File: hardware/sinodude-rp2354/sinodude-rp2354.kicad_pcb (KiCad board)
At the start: 2 copper layers, 0 parts

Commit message: hardware: PCB placement, 2-layer stackup and ground pours
75 x 40 mm two-layer board. J1 (USB-C), U1 (RP2354A) and J4 (DUT IDC header)
share the y=120 centreline, with signal flow left to right: USB-C, ESD, MCU,
level shifters, DUT header.

U1 is rotated 180 so its pins 4-14 (the nine level-shifter signals, the widest
bundle on the board) face U4 directly, and USB DM/DP leave the bottom-left
toward J1. Decoupling rings U1 on all four sides; the B-side series resistors
and ESD diodes stack in two columns between U4 and J4.

Netclasses follow Glasgow's revC3 values scaled for 2 layers: Default 0.2 mm
track / 0.2 mm clearance / 0.6-0.3 via, Power 0.5 mm, Fine 0.15 mm for the
0.4 mm-pitch QFN escapes. GND pours on both layers.

Placement scores clean on courtyards; the two reported outline failures are
J1 and J4 deliberately overhanging, being the USB-C mouth and the IDC shroud.
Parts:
- added C1: 100nF, Capacitor_SMD:C_0402_1005Metric, F.Cu at (108.5, 110.0)
- added C10: 100nF, Capacitor_SMD:C_0402_1005Metric, F.Cu at (131.1, 125.0)
- added C11: 100nF, Capacitor_SMD:C_0402_1005Metric, F.Cu at (133.3, 125.0)
- added C12: 100nF, Capacitor_SMD:C_0402_1005Metric, F.Cu at (125.2, 117.5)
- added C13: 100nF, Capacitor_SMD:C_0402_1005Metric, F.Cu at (134.8, 120.0)
- added C14: 100nF, Capacitor_SMD:C_0402_1005Metric, F.Cu at (129.9, 115.0)
- added C15: 100nF, Capacitor_SMD:C_0402_1005Metric, F.Cu at (125.2, 120.0)
- added C16: 100nF, Capacitor_SMD:C_0402_1005Metric, F.Cu at (134.8, 117.5)
- added C17: 100nF, Capacitor_SMD:C_0402_1005Metric, F.Cu at (134.8, 122.5)
- added C18: 100nF, Capacitor_SMD:C_0402_1005Metric, F.Cu at (125.2, 122.5)
- added C19: 10uF/6.3V/20%/X5R/C0402, Capacitor_SMD:C_0402_1005Metric, F.Cu at (136.8, 124.5)
- added C20: 4.7uF/10V/20%/X5R/C0402, Capacitor_SMD:C_0402_1005Metric, F.Cu at (126.7, 125.0)
- added C21: 4.7uF/10V/20%/X5R/C0402, Capacitor_SMD:C_0402_1005Metric, F.Cu at (119.5, 127.0)
- added C22: 15pF/50V/5%/C0G/C0603, Capacitor_SMD:C_0603_1608Metric, F.Cu at (126.0, 111.3)
- added C23: 15pF/50V/5%/C0G/C0603, Capacitor_SMD:C_0603_1608Metric, F.Cu at (135.0, 111.3)
- added C25: 100nF, Capacitor_SMD:C_0402_1005Metric, F.Cu at (121.5, 105.0)
- added C26: 100nF, Capacitor_SMD:C_0402_1005Metric, F.Cu at (121.0, 135.0)
- added C27: 10uF, Capacitor_SMD:C_0805_2012Metric, F.Cu at (148.0, 131.0)
- added C28: 100nF, Capacitor_SMD:C_0402_1005Metric, F.Cu at (152.5, 134.5)
- added C29: 100nF, Capacitor_SMD:C_0603_1608Metric, F.Cu at (130.5, 133.0)
- added C30: 100nF, Capacitor_SMD:C_0402_1005Metric, F.Cu at (140.0, 111.5)
- added C31: 100nF, Capacitor_SMD:C_0402_1005Metric, F.Cu at (149.0, 111.5)
- added C32: 100nF, Capacitor_SMD:C_0402_1005Metric, F.Cu at (145.0, 124.0)
- added C33: 100nF, Capacitor_SMD:C_0402_1005Metric, F.Cu at (145.0, 131.0)
- added C34: 100nF, Capacitor_SMD:C_0402_1005Metric, F.Cu at (151.0, 124.0)
- added C35: 100nF, Capacitor_SMD:C_0402_1005Metric, F.Cu at (151.0, 131.0)
- added C36: 100nF, Capacitor_SMD:C_0603_1608Metric, F.Cu at (155.0, 130.0)
- added C37: 4.7uF/10V/20%/X5R/C0402, Capacitor_SMD:C_0402_1005Metric, F.Cu at (128.9, 125.0)
- added C4: 10uF, Capacitor_SMD:C_0805_2012Metric, F.Cu at (117.5, 105.0)
- added C5: 22uF, Capacitor_SMD:C_1206_3216Metric, F.Cu at (121.0, 131.5)
- added C6: 100nF, Capacitor_SMD:C_0402_1005Metric, F.Cu at (125.5, 115.0)
- added C7: 100nF, Capacitor_SMD:C_0402_1005Metric, F.Cu at (127.7, 115.0)
- added C8: 100nF, Capacitor_SMD:C_0402_1005Metric, F.Cu at (132.1, 115.0)
- added C9: 100nF, Capacitor_SMD:C_0402_1005Metric, F.Cu at (134.3, 115.0)
- added D1: USBLC6-2SC6, Package_TO_SOT_SMD:SOT-23-6, F.Cu at (112.5, 120.0)
- added D2: GRN, LED_SMD:LED_0603_1608Metric, F.Cu at (136.0, 105.5)
- added D3: RED, LED_SMD:LED_0603_1608Metric, F.Cu at (139.5, 105.5)
- added D4: H5VSD3B/VRWM5V/SOD-323, Diode_SMD:D_SOD-323, F.Cu at (158.2, 112.0)
- added D5: H5VSD3B/VRWM5V/SOD-323, Diode_SMD:D_SOD-323, F.Cu at (158.2, 115.0)
- added D6: H5VSD3B/VRWM5V/SOD-323, Diode_SMD:D_SOD-323, F.Cu at (158.2, 118.0)
- added D7: H5VSD3B/VRWM5V/SOD-323, Diode_SMD:D_SOD-323, F.Cu at (158.2, 121.0)
- added D8: H5VSD3B/VRWM5V/SOD-323, Diode_SMD:D_SOD-323, F.Cu at (158.2, 124.0)
- added F1: 500mA/Rmax300mR/F1206, Fuse:Fuse_1206_3216Metric, F.Cu at (112.0, 105.0)
- added FB1: 600R@100MHz, Resistor_SMD:R_0603_1608Metric, F.Cu at (122.0, 115.0)
- added H1: MountingHole, MountingHole:MountingHole_2.7mm_M2.5, F.Cu at (105.0, 105.0)
- added H2: MountingHole, MountingHole:MountingHole_2.7mm_M2.5, F.Cu at (170.0, 105.0)
- added H3: MountingHole, MountingHole:MountingHole_2.7mm_M2.5, F.Cu at (105.0, 135.0)
- added H4: MountingHole, MountingHole:MountingHole_2.7mm_M2.5, F.Cu at (170.0, 135.0)
- added J1: USB-C, Connector_USB:USB_C_Receptacle_GCT_USB4105-xx-A_16P_TopMnt_Horizontal, F.Cu at (103.7, 120.0)
- added J2: SWD TC2030, Connector:Tag-Connect_TC2030-IDC-NL_2x03_P1.27mm_Vertical, F.Cu at (117.0, 109.5)
- added J4: DUT, Connector_IDC:IDC-Header_2x05_P2.54mm_Horizontal, F.Cu at (161.7, 114.9)
- added L1: 3.3uH/20%/Isat2.4A/DCR140m/POL, sinodude:L_Abracon_AOTA-B201610S_0806_2016Metric_Polarized, F.Cu at (123.5, 127.0)
- added Q1: 2N7002, Package_TO_SOT_SMD:SOT-23, F.Cu at (156.0, 133.0)
- added R1: 5k1, Resistor_SMD:R_0603_1608Metric, F.Cu at (111.5, 115.5)
- added R10: 470R, Resistor_SMD:R_0603_1608Metric, F.Cu at (139.5, 108.5)
- added R13: 10k, Resistor_SMD:R_0603_1608Metric, F.Cu at (148.5, 134.5)
- added R14: 10k, Resistor_SMD:R_0603_1608Metric, F.Cu at (145.0, 137.5)
- added R15: 750R/1%/ILIM333mA, Resistor_SMD:R_0603_1608Metric, F.Cu at (140.0, 137.5)
- added R16: 10k, Resistor_SMD:R_0603_1608Metric, F.Cu at (149.0, 137.5)
- added R17: 10k, Resistor_SMD:R_0603_1608Metric, F.Cu at (128.0, 131.0)
- added R18: 10k, Resistor_SMD:R_0603_1608Metric, F.Cu at (131.0, 131.0)
- added R19: 1k, Resistor_SMD:R_0603_1608Metric, F.Cu at (161.5, 136.5)
- added R2: 5k1, Resistor_SMD:R_0603_1608Metric, F.Cu at (111.5, 124.5)
- added R20: 100k, Resistor_SMD:R_0603_1608Metric, F.Cu at (165.0, 136.5)
- added R21: 150R/1%/250mW/R1206, Resistor_SMD:R_1206_3216Metric, F.Cu at (156.0, 136.5)
- added R22: 10k, Resistor_SMD:R_0603_1608Metric, F.Cu at (140.0, 122.5)
- added R23: 10k, Resistor_SMD:R_0603_1608Metric, F.Cu at (141.0, 125.0)
- added R24: 10k, Resistor_SMD:R_0603_1608Metric, F.Cu at (148.0, 124.0)
- added R25: 22R, Resistor_SMD:R_0603_1608Metric, F.Cu at (154.5, 112.0)
- added R26: 22R, Resistor_SMD:R_0603_1608Metric, F.Cu at (154.5, 115.0)
- added R27: 22R, Resistor_SMD:R_0603_1608Metric, F.Cu at (154.5, 118.0)
- added R28: 22R, Resistor_SMD:R_0603_1608Metric, F.Cu at (154.5, 121.0)
- added R29: 10k, Resistor_SMD:R_0603_1608Metric, F.Cu at (161.5, 133.0)
- added R3: 27R, Resistor_SMD:R_0603_1608Metric, F.Cu at (117.0, 122.5)
- added R30: 22R, Resistor_SMD:R_0603_1608Metric, F.Cu at (154.5, 124.0)
- added R31: 10k, Resistor_SMD:R_0603_1608Metric, F.Cu at (165.0, 133.0)
- added R32: 330R, Resistor_SMD:R_0603_1608Metric, F.Cu at (155.0, 127.0)
- added R33: 10k, Resistor_SMD:R_0603_1608Metric, F.Cu at (158.5, 127.0)
- added R4: 27R, Resistor_SMD:R_0603_1608Metric, F.Cu at (117.0, 117.5)
- added R5: 33R/1%/R0402, Resistor_SMD:R_0402_1005Metric, F.Cu at (128.0, 128.0)
- added R6: 1k, Resistor_SMD:R_0603_1608Metric, F.Cu at (137.5, 112.0)
- added R7: 1k, Resistor_SMD:R_0603_1608Metric, F.Cu at (137.0, 128.0)
- added R8: 10k, Resistor_SMD:R_0603_1608Metric, F.Cu at (122.0, 112.0)
- added R9: 470R, Resistor_SMD:R_0603_1608Metric, F.Cu at (136.0, 108.5)
- added SW1: BOOTSEL, Button_Switch_SMD:SW_Push_1P1T_NO_CK_KMR2, F.Cu at (135.0, 136.0)
- added SW2: RESET, Button_Switch_SMD:SW_Push_1P1T_NO_CK_KMR2, F.Cu at (127.0, 136.0)
- added U1: RP2354A, sinodude:QFN-60-1EP_7x7mm_P0.4mm_EP3.4x3.4mm_ThermalVias, F.Cu at (130.0, 120.0)
- added U2: AMS1117-3.3, Package_TO_SOT_SMD:SOT-223-3_TabPin2, F.Cu at (113.0, 131.0)
- added U3: TPS2114APW, Package_SO:TSSOP-8_4.4x3mm_P0.65mm, F.Cu at (142.0, 134.5)
- added U4: SN74LVC8T245PW, Package_SO:TSSOP-24_4.4x7.8mm_P0.65mm, F.Cu at (144.5, 117.0)
- added U5: SN74LVC1T45DBV, Package_TO_SOT_SMD:SOT-23-6, F.Cu at (145.0, 127.5)
- added U6: SN74LVC1T45DBV, Package_TO_SOT_SMD:SOT-23-6, F.Cu at (151.0, 127.5)
- added Y1: 12MHz/CL10pF/ESR50R/ABM8-272-T3, Crystal:Crystal_SMD_3225-4Pin_3.2x2.5mm, F.Cu at (130.6, 111.3)
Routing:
- added copper zone on B.Cu, net GND
- added copper zone on F.Cu, net GND
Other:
- board outline added: 75 x 40 mm

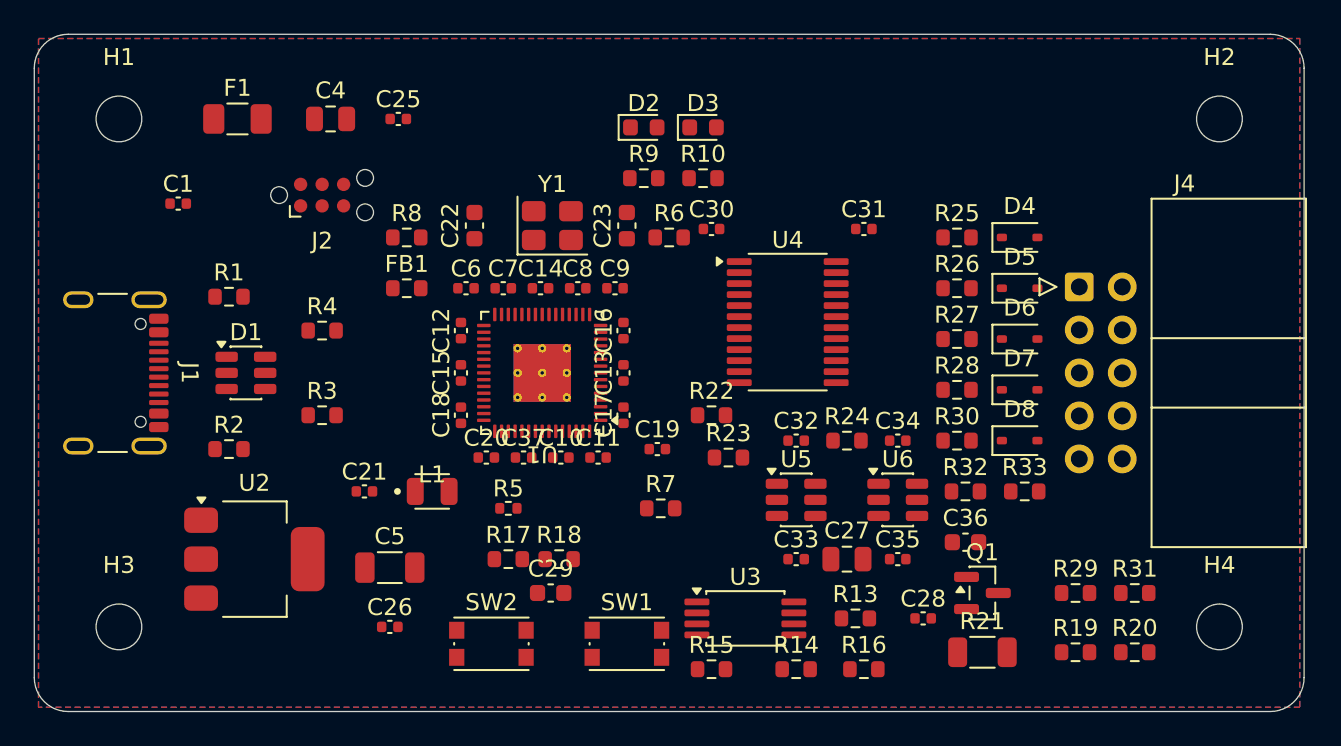
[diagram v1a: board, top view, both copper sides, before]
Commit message: hardware: 0603 passives, both-sides placement, latching Tag-Connect
Standardise R and C on 0603, keeping three exceptions where the package is
load-bearing: R21 (1206, ~167 mW), C5 (1206, 22uF bulk) and C4/C27 (0805,
10uF bulk). Re-sourced the four affected part numbers as Basic-library 0603
parts; the 10uF gains 6.3V->10V and the 4.7uF 10V->16V along the way.

Move decoupling and pull-ups to the bottom side, under the IC they serve: on
two layers that is what frees the top for signal routing and shortens each
decoupling loop to a via. 44 parts on top, 49 on bottom. Series resistors in
signal paths stay on top where the trace already runs.

J2 becomes the latching TC2030-IDC-FP so the probe holds itself in place; it
is 8.0 x 8.5 mm against the no-legs 7.0 x 4.0 and needed relocating.

Placement is clean on same-side courtyards. The two reported outline failures
are J1 and J4 overhanging on purpose, being the USB-C mouth and IDC shroud.
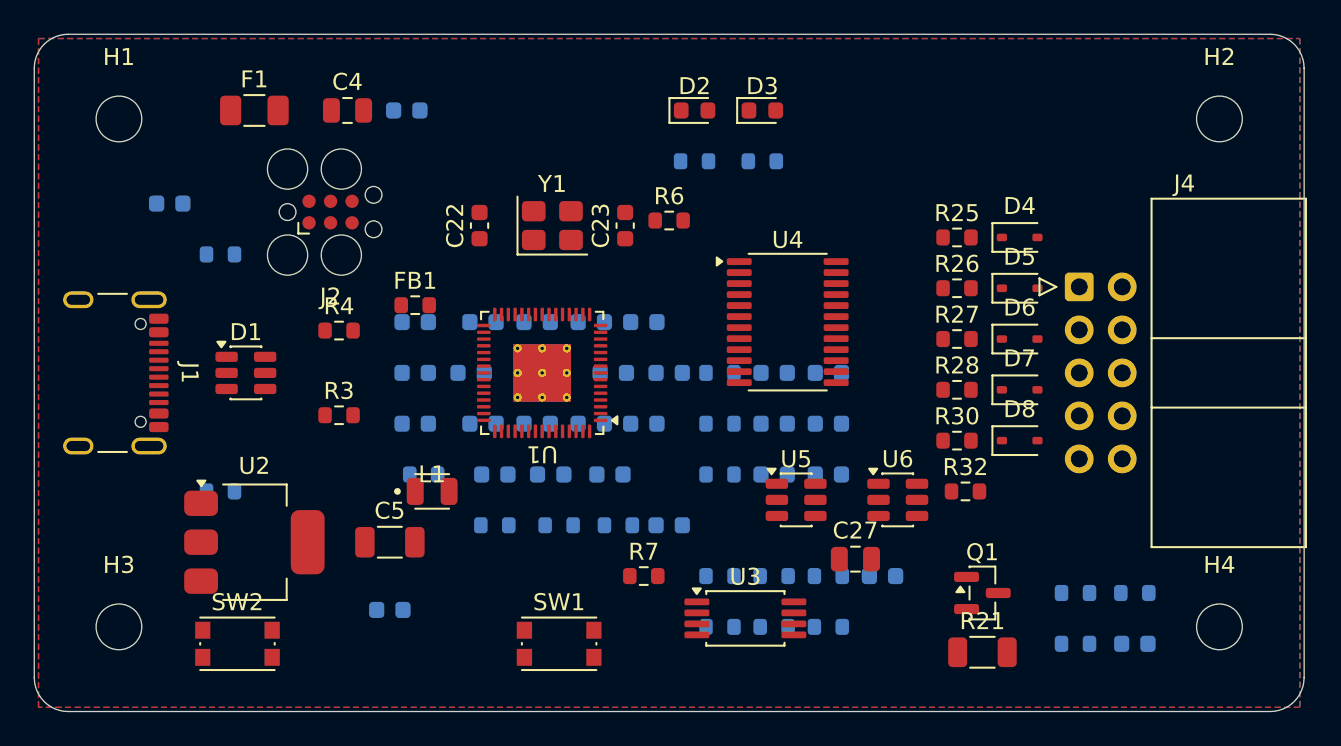
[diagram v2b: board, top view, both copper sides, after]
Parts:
- C1, C10, C11, C12, C13, C14, C15, C16, C17, C18, C25, C26, C28, C30, C31, C32, C33, C34, C35, C6, C7, C8, C9: footprint Capacitor_SMD:C_0402_1005Metric -> Capacitor_SMD:C_0603_1608Metric; moved to B.Cu
- C19: value 10uF/6.3V/20%/X5R/C0402 -> 10uF/10V/10%/X5R/C0603; footprint Capacitor_SMD:C_0402_1005Metric -> Capacitor_SMD:C_0603_1608Metric; moved to B.Cu
- C20, C21, C37: value 4.7uF/10V/20%/X5R/C0402 -> 4.7uF/16V/10%/X5R/C0603; footprint Capacitor_SMD:C_0402_1005Metric -> Capacitor_SMD:C_0603_1608Metric; moved to B.Cu
- C29, C36, R1, R10, R13, R14, R15, R16, R17, R18, R19, R2, R20, R22, R23, R24, R29, R31, R33, R8, R9: moved to B.Cu
- J2: value SWD TC2030 -> SWD TC2030-IDC latching; footprint Connector:Tag-Connect_TC2030-IDC-NL_2x03_P1.27mm_Vertical -> Connector:Tag-Connect_TC2030-IDC-FP_2x03_P1.27mm_Vertical
- R5: value 33R/1%/R0402 -> 33R/1%/R0603; footprint Resistor_SMD:R_0402_1005Metric -> Resistor_SMD:R_0603_1608Metric; moved to B.Cu
- moved R20 18.2 mm to (146.9, 135.0)
- moved R19 17.9 mm to (143.7, 135.0)
- moved SW2 15.0 mm to (112.0, 136.0)
- moved R8 14.0 mm to (123.0, 126.0)
- moved C36 11.7 mm to (165.0, 136.0)
- moved C9 11.2 mm to (126.5, 123.0)
- moved C21 11.0 mm to (130.5, 126.0)
- moved R33 9.49 mm to (161.5, 136.0)
- moved C30 9.27 mm to (143.7, 120.0)
- moved C13 9.00 mm to (125.8, 120.0), turned to 0 degrees
- moved R16 8.86 mm to (140.5, 135.0)
- moved R15 8.82 mm to (146.9, 132.0)
- moved C31 8.76 mm to (146.9, 120.0)
- moved R13 8.38 mm to (140.5, 132.0)
- moved C29 8.06 mm to (137.5, 129.0)
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
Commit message: hardware: M3 mounting holes, U1 decoupling back to top side
Mounting holes go M2.5 -> M3 (3.2 mm drill), inset to clear U2 and J4.

Move U1's decoupling back to the top, ringed around the package. Building the
net map showed why the bottom-side version could not work: the QFN's pad rows
sit directly above the bottom cap pads, so a via at a cap would land under
pins 25/26 (SWDIO/RUN). QFN-60 is peripheral-only, so a top-side ring reaches
every rail pin with a direct trace and no via in the decoupling loop at all.

Pull-ups, LED and CC resistors, and the non-U1 bypass caps stay on the bottom.

Also nudged for routing: R6 beside the crystal instead of 9 mm from XOUT, R7
between U1 and SW1, R1/R2 against J1's CC pads, the VTGT sense divider onto
the VTGT cluster, and R19/R20 next to Q1's gate.
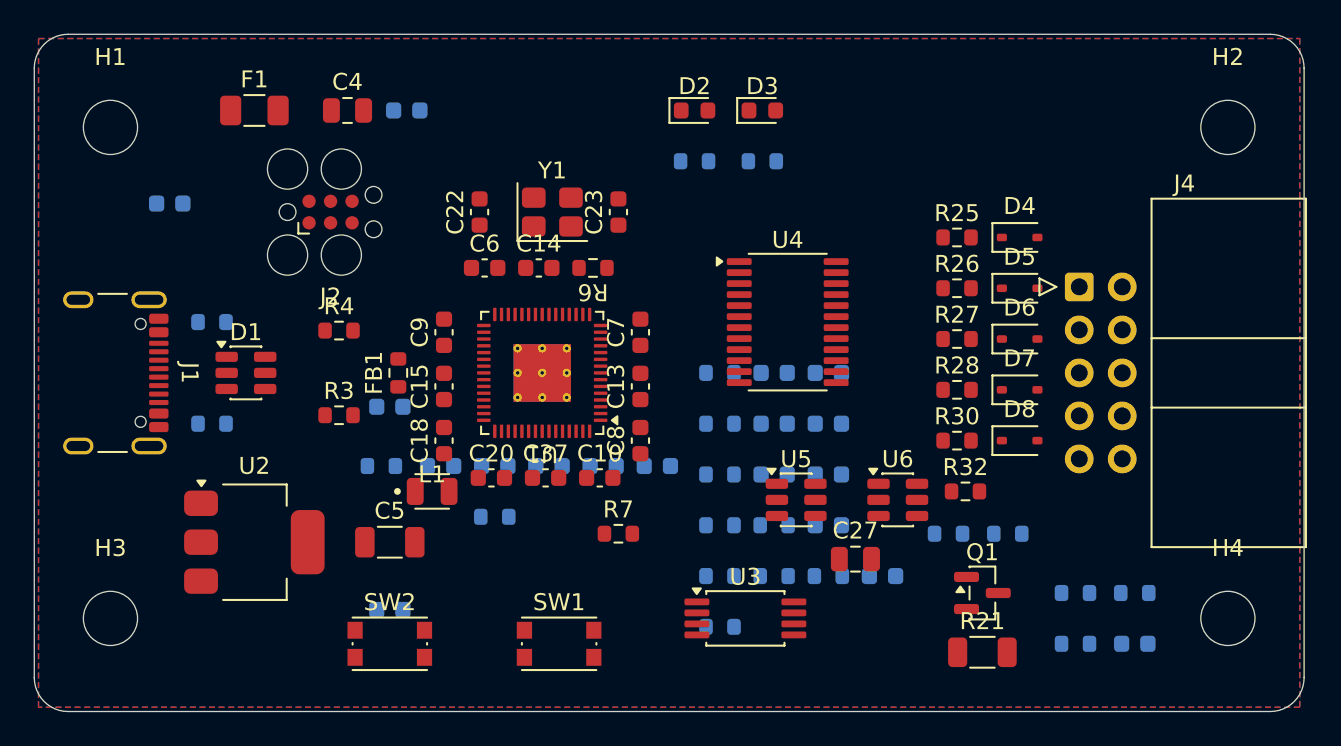
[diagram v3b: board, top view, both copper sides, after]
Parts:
- C10, C13, C14, C15, C18, C20, C37, C6, C7, C8, C9: moved to F.Cu
- H1, H2, H3, H4: value MountingHole -> MountingHole M3; footprint MountingHole:MountingHole_2.7mm_M2.5 -> MountingHole:MountingHole_3.2mm_M3
- moved R20 11.9 mm to (157.5, 129.5)
- moved R19 11.7 mm to (154.0, 129.5)
- moved C21 10.3 mm to (121.0, 122.0)
- moved C16 10.2 mm to (130.4, 125.5)
- moved C13 10.0 mm to (135.8, 120.8), turned to 90 degrees
- moved C12 9.71 mm to (127.2, 125.5)
- moved R17 9.50 mm to (140.5, 129.0)
- moved C29 9.40 mm to (146.9, 129.0)
- moved C11 9.24 mm to (124.0, 125.5)
- moved R18 9.20 mm to (143.7, 129.0)
- moved SW2 9.00 mm to (121.0, 136.0)
- moved C14 7.60 mm to (129.8, 113.8)
- moved C8 7.58 mm to (135.8, 124.0), turned to 90 degrees
- moved C7 6.13 mm to (135.8, 117.6), turned to 90 degrees
- moved C9 5.87 mm to (124.2, 117.6), turned to 90 degrees
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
